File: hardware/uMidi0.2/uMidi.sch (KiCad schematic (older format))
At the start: 43 parts, among them CON1 USB-MINI-B, IC1 6N138, IC2 ATXMEGA128A4U-M, P1 MIDI In, P2 MIDI Thru, P3 MIDI T/O, P4 MIDI Out, P5 5..12 V, P6 PDI, P7 GPIO1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

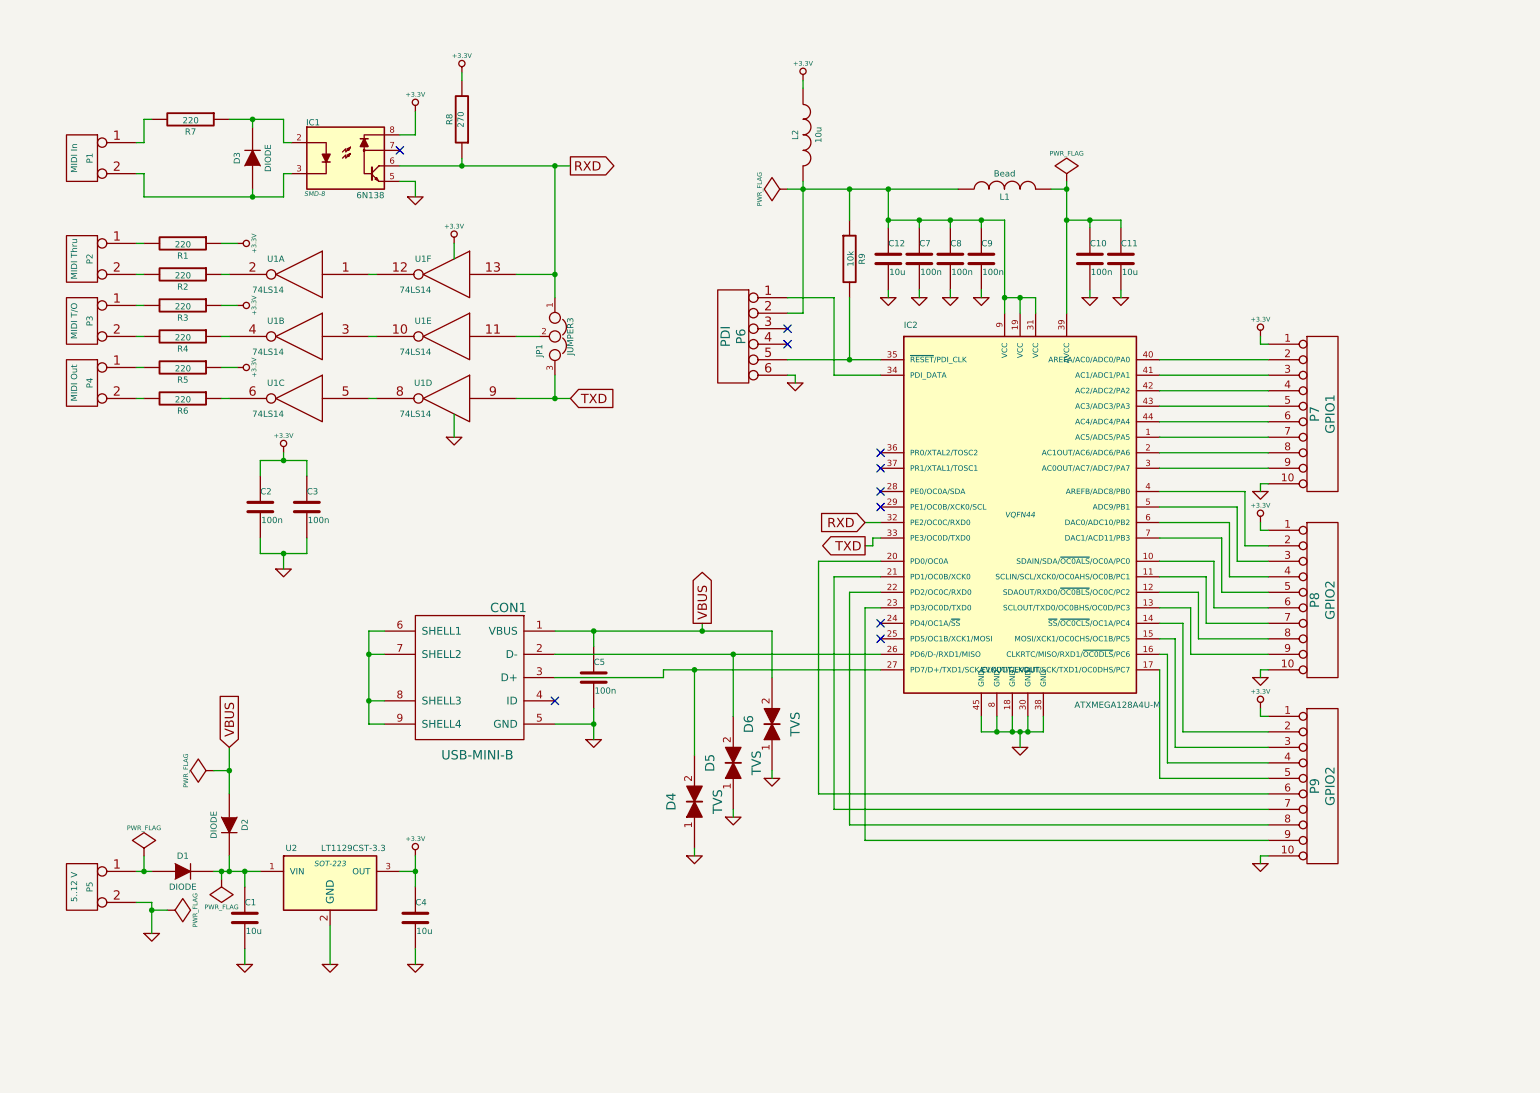
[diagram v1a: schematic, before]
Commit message: Add filter network between USB shield and GND
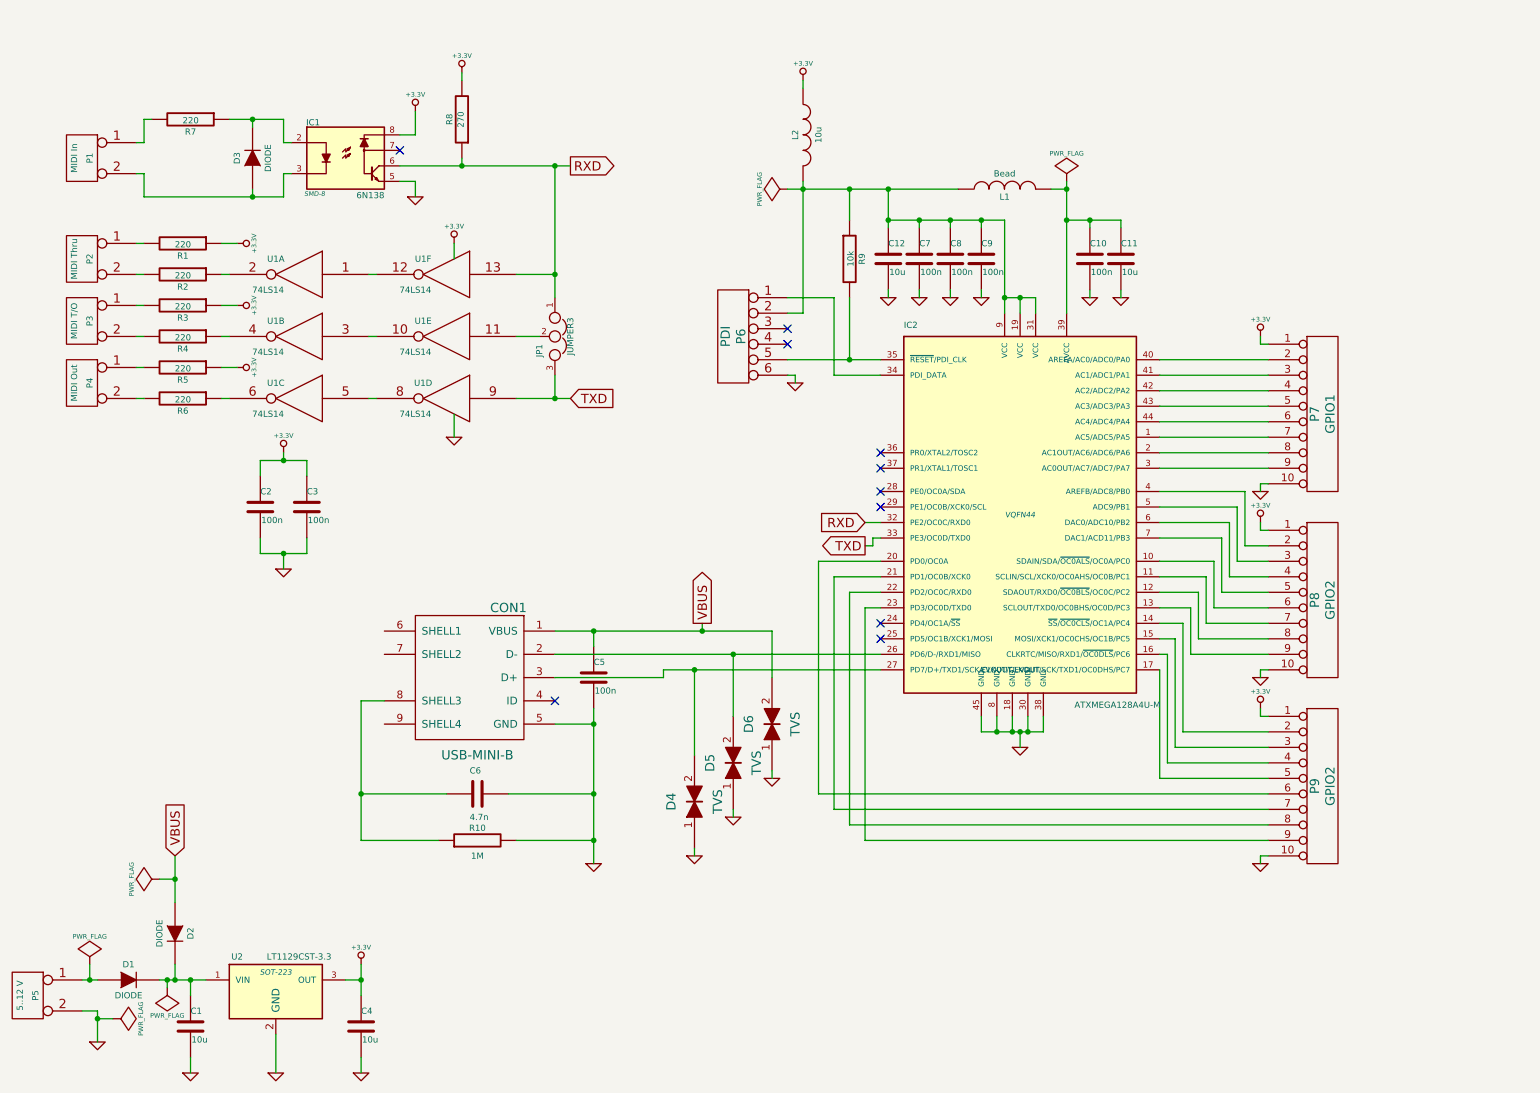
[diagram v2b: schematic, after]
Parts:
- added C6: 4.7n, symbol C
- added R10: 1M, symbol R
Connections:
- net GND: now also C6.1, R10.2
- new net: C6.2, CON1.8 (SHELL3), R10.1
- now unconnected: CON1.6 (SHELL1), CON1.7 (SHELL2), CON1.9 (SHELL4)
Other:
- moved on the sheet: C1, C4, D1, D2, P5, U2

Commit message: Add filters to GPIO pwr supply
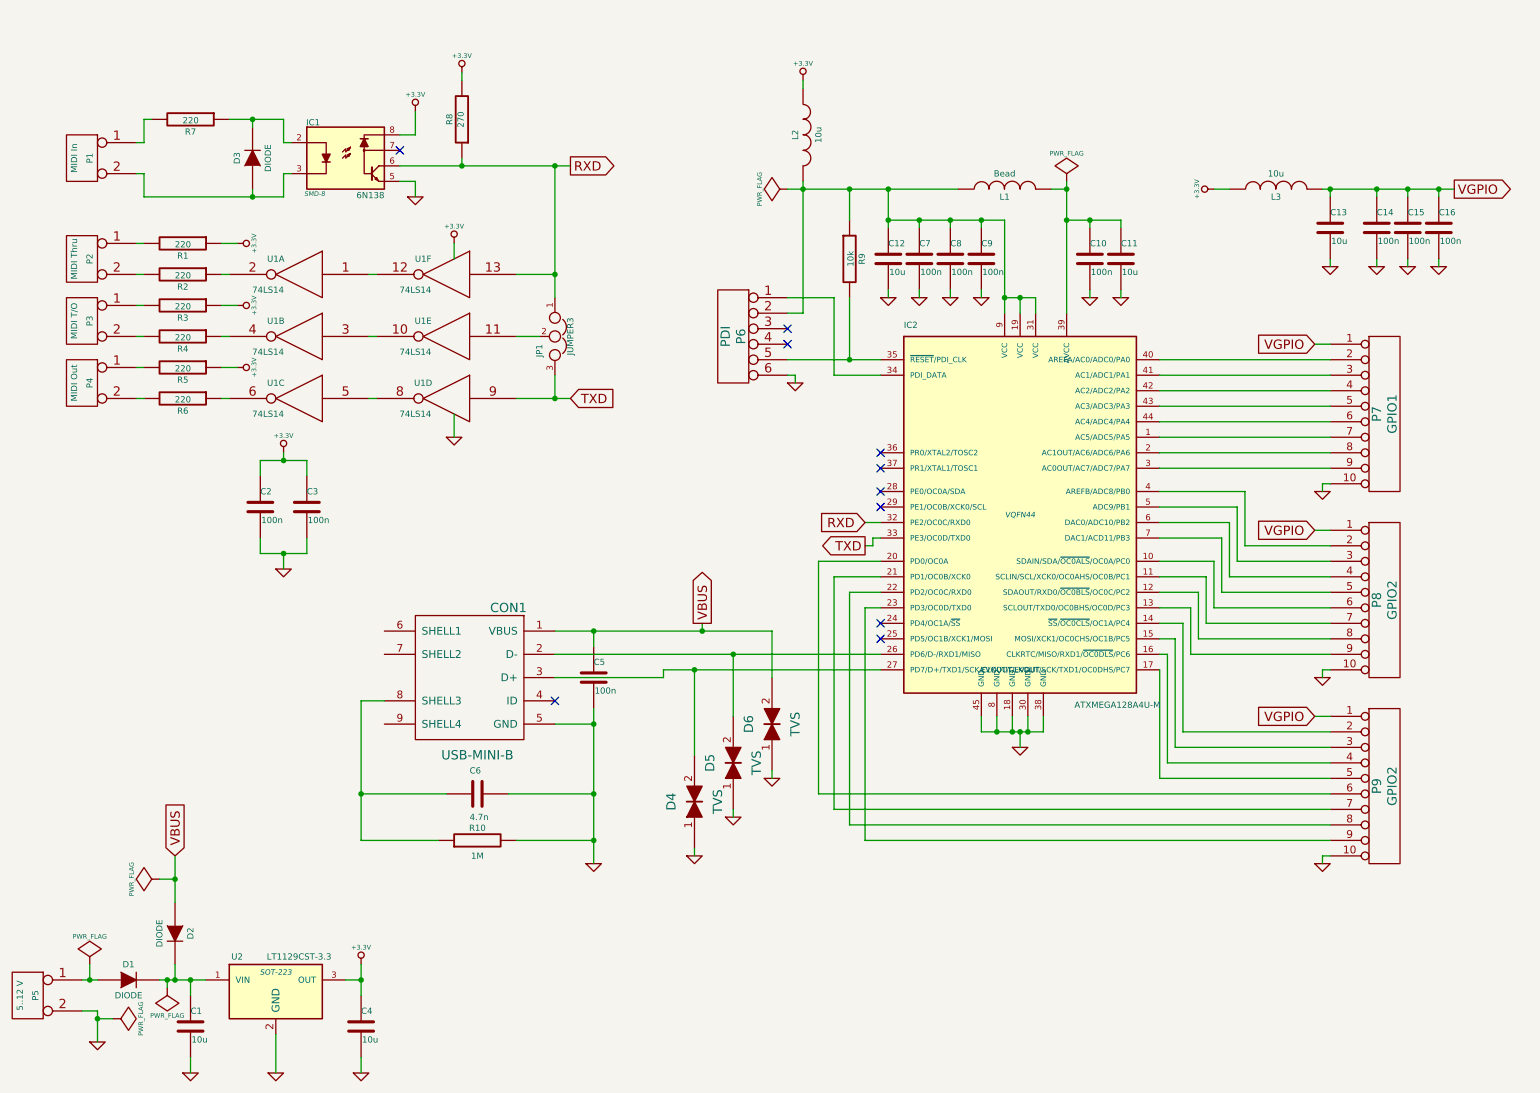
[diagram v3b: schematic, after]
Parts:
- added C13: 10u, symbol C
- added C14, C15, C16: 100n, symbol C
- added L3: 10u, symbol INDUCTOR
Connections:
- net +3.3V: now also L3.1; no longer P7.1 (P1), P8.1 (P1), P9.1 (P1)
- net GND: now also C13.2, C14.2, C15.2, C16.2
- new net VGPIO: C13.1, C14.1, C15.1, C16.1, L3.2, P7.1 (P1), P8.1 (P1), P9.1 (P1)
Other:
- moved on the sheet: P7, P8, P9

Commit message: Add debugging and testing LEDs
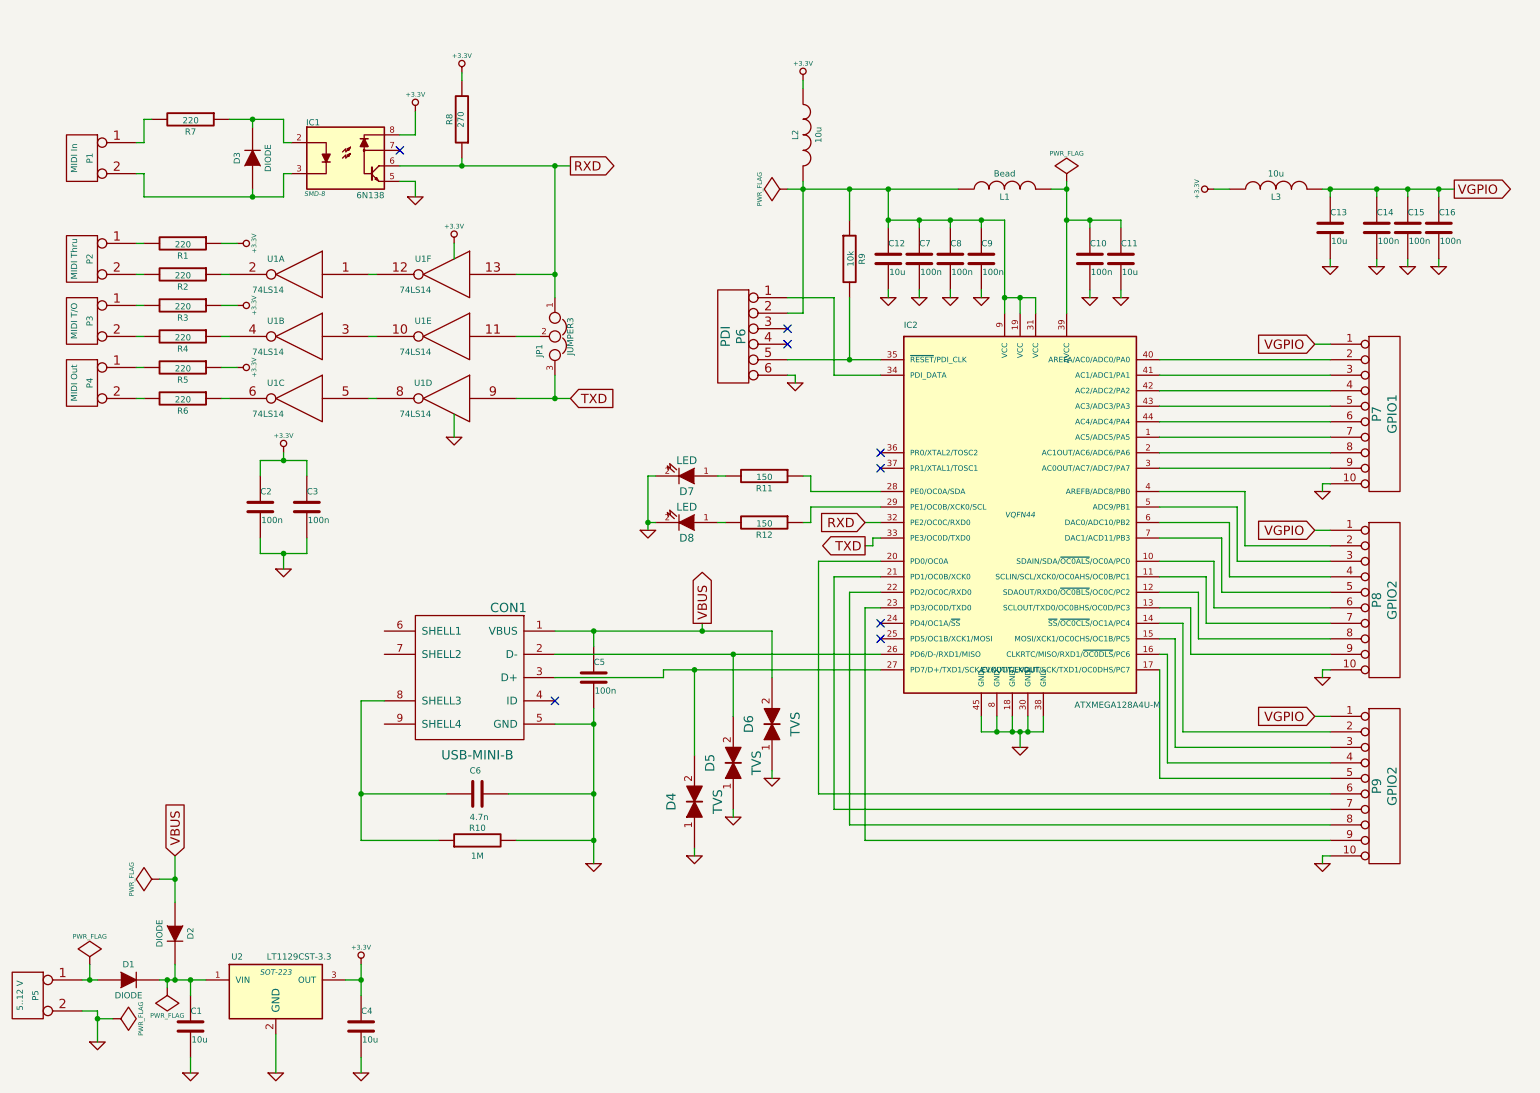
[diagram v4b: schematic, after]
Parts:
- added D7, D8: LED, symbol LED
- added R11, R12: 150, symbol R
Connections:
- net GND: now also D7.2 (K), D8.2 (K)
- net at IC2.28 (PE0/OC0A/SDA): now also R11.1
- net at IC2.29 (PE1/OC0B/XCK0/SCL): now also R12.1
- new net: D7.1 (A), R11.2
- new net: D8.1 (A), R12.2
- no-connect marks 10 -> 8

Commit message: Add optocoupler base pulldown (signal integrity)
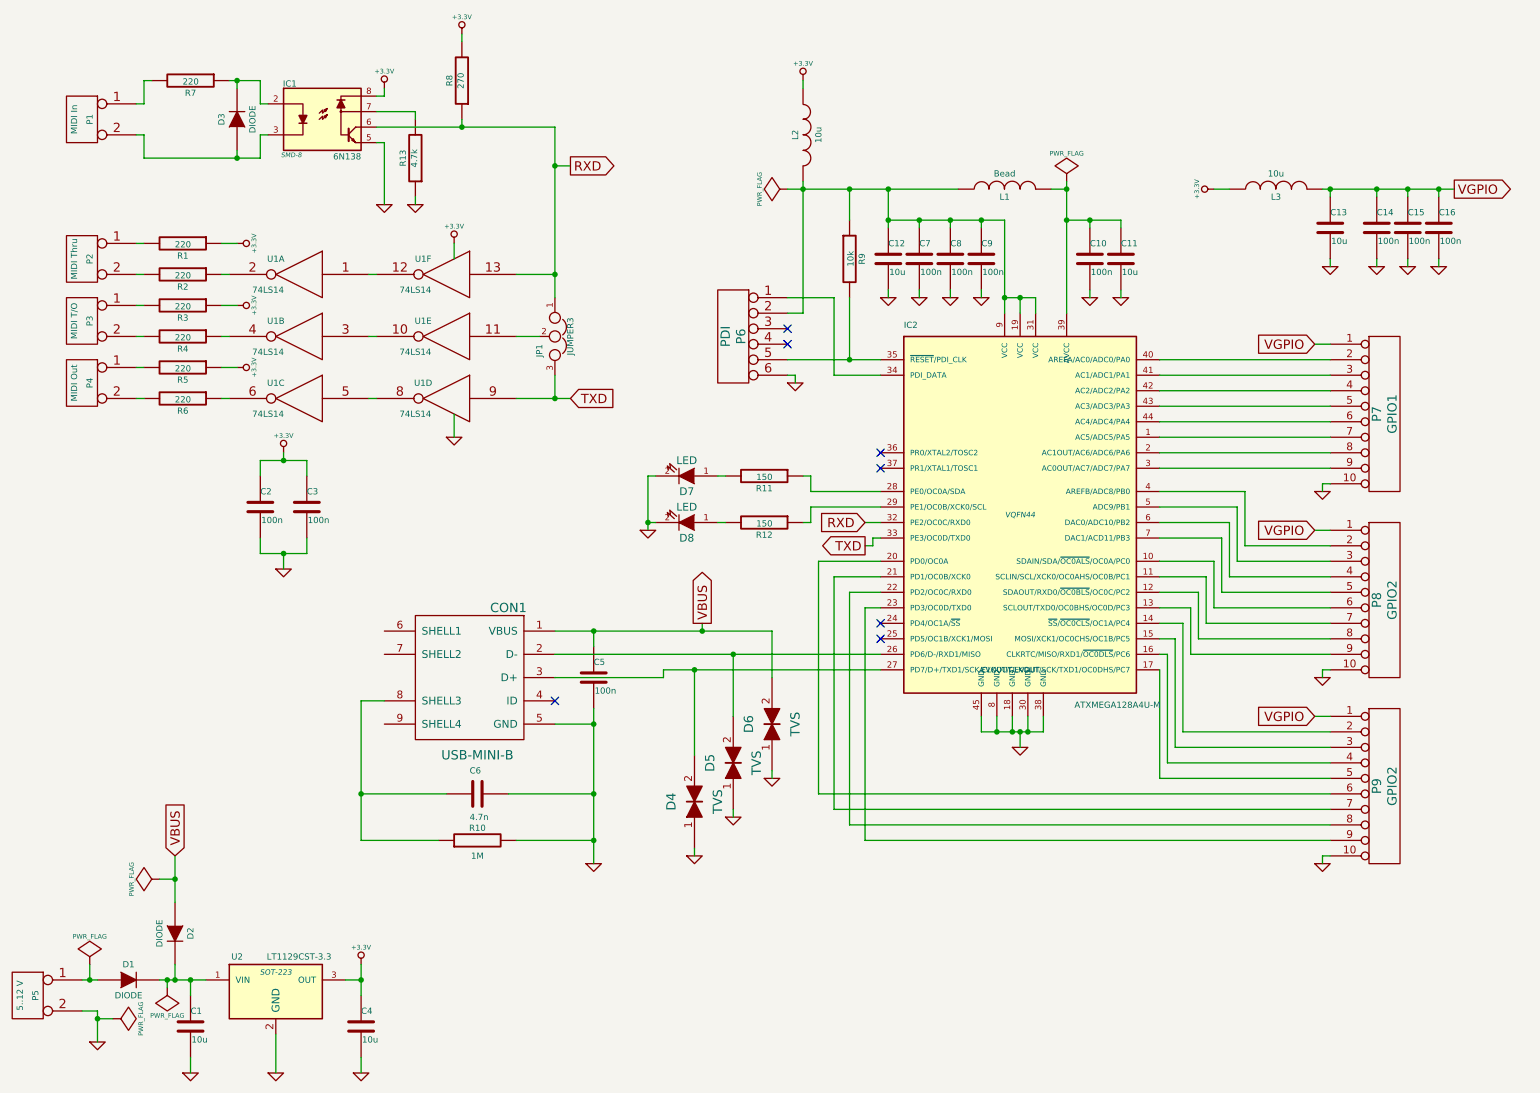
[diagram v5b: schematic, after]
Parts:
- added R13: 4.7k, symbol R
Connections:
- net GND: now also R13.1
- net at IC1.7: now also R13.2
- no-connect marks 8 -> 7
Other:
- moved on the sheet: D3, IC1, P1, R7, R8
